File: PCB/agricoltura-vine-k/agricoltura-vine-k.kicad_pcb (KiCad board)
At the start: 4 copper layers, 110 x 80 mm, 110 parts, among them K1 G5LE-14_DC5, K2 G5LE-14_DC5, K3 G5LE-14_DC5, K4 G5LE-14_DC5, Q1 IRLML6346TRPBF, Q2 IRLML6346TRPBF, Q3 IRLML6346TRPBF, Q4 IRLML6346TRPBF, SW1 TL3301NF260QG, T1 BU2032SM-JJ-GTR, T16 0395121002, T17 0395121004, T18 0395121004, T19 TSW-108-07-G-T, T2 20021121-00010C4LF, T20 0010897080, T3 0675031020, T4 0395121006, T5 0395121006, U1 STM32F446RET6, U10 ZXGD3009E6TA, U2 ZXGD3009E6TA, U3 ZXGD3009E6TA, U4 AP63203WU-7, U5 AP63205WU-7, U6 MAX13450EAUD+, U7 MAX13450EAUD+, U8 TCA6416ARTWR, U9 ZXGD3009E6TA, X1 ABM3B-8.000MHZ-B2-T, X2 ABS07-32.768KHZ-9-T

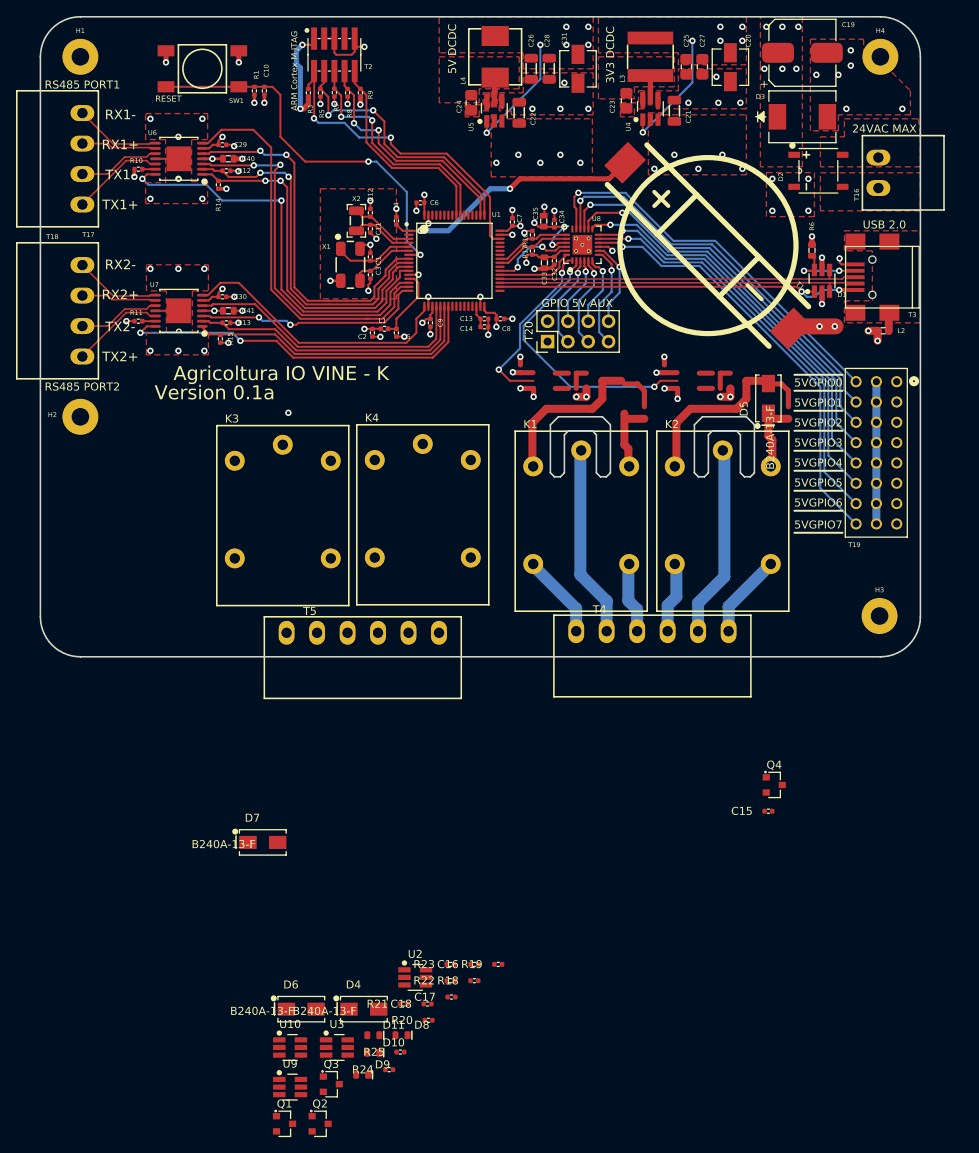
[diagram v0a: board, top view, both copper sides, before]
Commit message: PCB Routing PRogress
5th relay added to schematic, PCB section with Relays routed, still need to connecto IO expander channels.
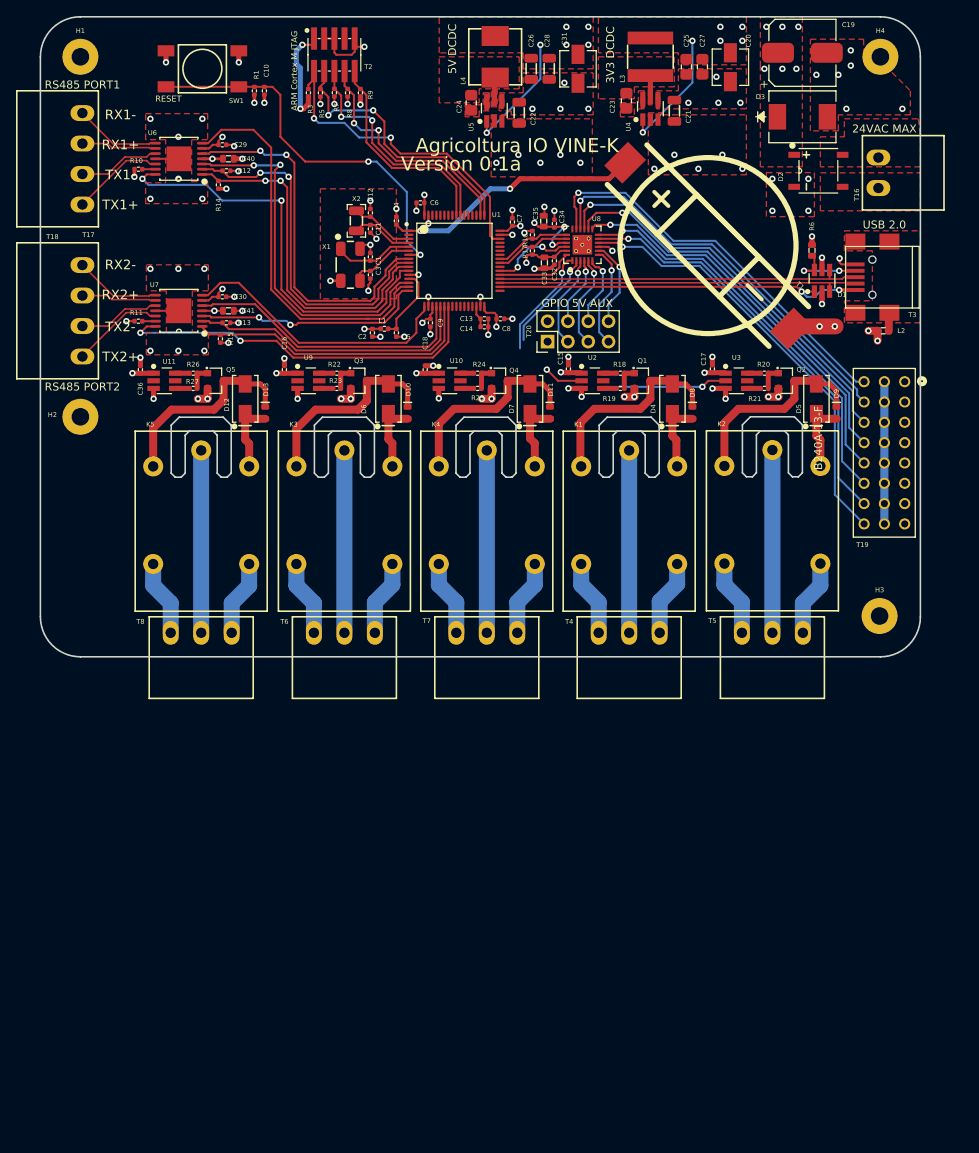
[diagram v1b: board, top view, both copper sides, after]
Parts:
- added C36: C0402C104K9PACTU, AVR-KiCAD-Lib-Resistors:R0402, F.Cu at (117.5, 104.1)
- added D12: B240A-13-F, AVR-KiCAD-Lib-Diodes:B240A-13-F, F.Cu at (130.6, 107.8)
- added D13: LTST-C194TBKT, AVR-KiCAD-Lib-Diodes:LED0603, F.Cu at (133.1, 109.5)
- added K5: G5LE-14_DC5, AVR-KiCAD-Lib-Relays-Contactors:G5LE-14_DC5, F.Cu at (125.1, 122.3)
- added Q5: IRLML6346TRPBF, AVR-KiCAD-Lib-Transistors:SOT-23, F.Cu at (126.9, 105.5)
- added R26: RC0402FR-0710RL, AVR-KiCAD-Lib-Resistors:R0402, F.Cu at (124.1, 104.5)
- added R27: RC0402FR-0710RL, AVR-KiCAD-Lib-Resistors:R0402, F.Cu at (124.1, 106.5)
- added T6: 0395121003, AVR-KiCAD-Lib-Connectors:0395121003, F.Cu at (143.0, 137.0)
- added T7: 0395121003, AVR-KiCAD-Lib-Connectors:0395121003, F.Cu at (160.8, 137.0)
- added T8: 0395121003, AVR-KiCAD-Lib-Connectors:0395121003, F.Cu at (125.1, 137.0)
- added U11: ZXGD3009E6TA, growbox-KiCAD-ICs:SOT-23-6_Handsoldering, F.Cu at (120.5, 105.5)
- T4, T5: value 0395121006 -> 0395121003; footprint AVR-KiCAD-Lib-Connectors:0395121006 -> AVR-KiCAD-Lib-Connectors:0395121003
- moved Q2 109.7 mm to (198.2, 105.5)
- moved Q1 103.1 mm to (180.2, 105.5)
- moved D9 101.8 mm to (204.5, 109.5), turned to 90 degrees
- moved U3 97.2 mm to (192.0, 105.5)
- moved R20 91.1 mm to (195.5, 104.5)
- moved R21 89.2 mm to (195.5, 106.5)
- moved U9 88.3 mm to (138.5, 105.5)
- moved Q3 88.0 mm to (144.8, 105.5)
- moved R24 87.8 mm to (159.7, 104.5)
- moved D8 85.9 mm to (186.5, 109.5), turned to 90 degrees
- moved U10 85.7 mm to (156.2, 105.5)
- moved D4 85.5 mm to (184.0, 107.8), turned to 90 degrees
- moved C17 85.0 mm to (189.0, 104.0), turned to 270 degrees
- moved R25 83.5 mm to (159.7, 106.5)
- moved D11 80.9 mm to (168.7, 109.5), turned to 90 degrees
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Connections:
- T5 pad 1: Net-(K3-Pad4) -> Net-(K2-Pad4)
- T5 pad 2: Net-(K3-Pad1) -> Net-(K2-Pad1)
- T5 pad 3: Net-(K3-Pad3) -> Net-(K2-Pad3)
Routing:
- net +5V: track 127.2 -> 189.3 mm, vias 13 -> 16
- net Net-(D12-Pad1): track 0.00 -> 25.3 mm
- net Net-(D10-Pad2): track 0.00 -> 25.2 mm
- net Net-(D11-Pad2): track 0.00 -> 25.2 mm
- net Net-(K5-Pad1): track 0.00 -> 22.8 mm
- net Net-(K4-Pad1): track 0.00 -> 22.8 mm
- net Net-(K3-Pad1): track 0.00 -> 22.8 mm
- net /5V IO Interfaces/DRV2: track 34.6 -> 12.7 mm, vias 2 -> 1
- net GND: track 83.0 -> 97.5 mm, vias 80 -> 92
- net /Relay Circuits/DRV2: track 0.00 -> 13.7 mm, vias 0 -> 1
- net Net-(K5-Pad4): track 0.00 -> 9.51 mm
- net Net-(K5-Pad3): track 0.00 -> 9.51 mm
- net Net-(K4-Pad4): track 0.00 -> 9.51 mm
- net Net-(K4-Pad3): track 0.00 -> 9.51 mm
- net Net-(K3-Pad4): track 0.00 -> 9.51 mm
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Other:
- outline, holes or cut-outs redrawn
- board text added: "Agricoltura IO VINE-K"
- board text removed: "5VGPIO0"
- board text removed: "5VGPIO1"
- board text removed: "5VGPIO2"
- board text removed: "5VGPIO3"
- board text removed: "5VGPIO4"
- board text removed: "5VGPIO5"
- board text removed: "5VGPIO6"
- board text removed: "5VGPIO7"
- board text removed: "Agricoltura IO VINE - K"

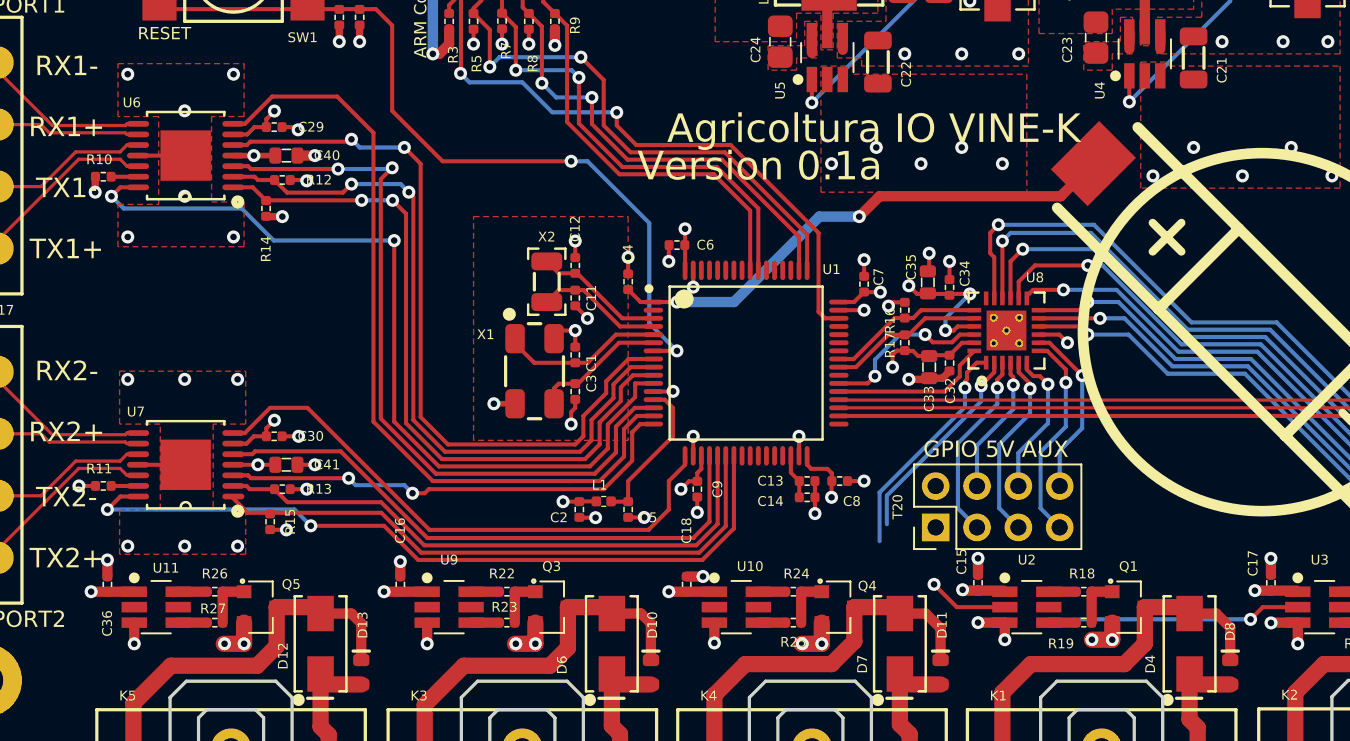
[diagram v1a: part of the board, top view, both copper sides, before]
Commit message: Finished
PCB routing complete, up for review before fab.
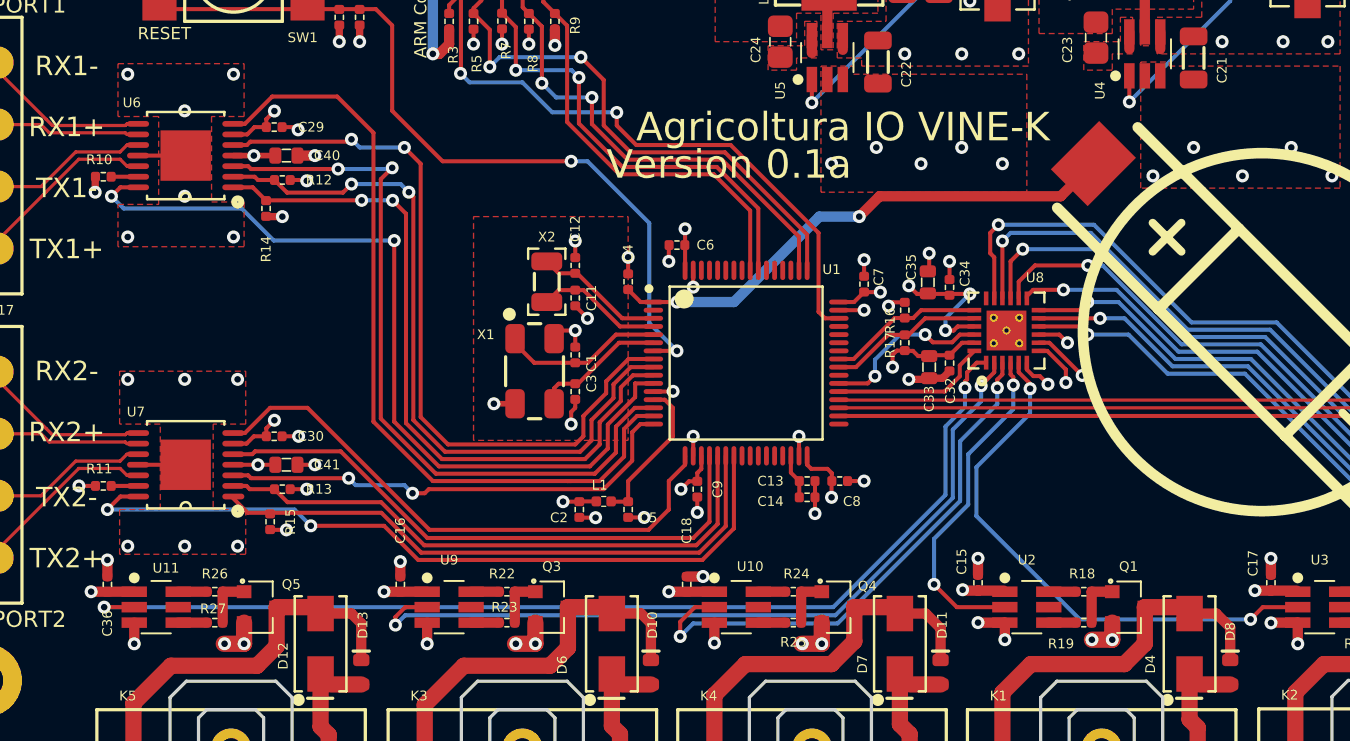
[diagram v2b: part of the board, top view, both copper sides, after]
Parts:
- removed T20: 0010897080, AVR-KiCAD-Lib-Connectors:Pin_Header_Straight_2x04_Pitch2.54mm
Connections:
- U10 pad 2: /Relay Circuits/DRV4 -> /5V IO Interfaces/DRV3
- U11 pad 2: Net-(U11-Pad2) -> /5V IO Interfaces/DRV5
- U2 pad 2: /Relay Circuits/DRV1 -> /5V IO Interfaces/DRV2
- U3 pad 2: /Relay Circuits/DRV2 -> /5V IO Interfaces/DRV1
- U8 pad 1: /5V IO Interfaces/DRV1 -> /5V IO Interfaces/DRV5
- U8 pad 2: /5V IO Interfaces/DRV2 -> /5V IO Interfaces/DRV4
- U8 pad 3: /5V IO Interfaces/P02 -> /5V IO Interfaces/DRV3
- U8 pad 4: /5V IO Interfaces/P03 -> /5V IO Interfaces/DRV2
- U8 pad 5: /5V IO Interfaces/P04 -> /5V IO Interfaces/DRV1
- U8 pad 6: /5V IO Interfaces/P05 -> Net-(U8-Pad6)
- U8 pad 7: /5V IO Interfaces/P06 -> Net-(U8-Pad7)
- U8 pad 8: /5V IO Interfaces/P07 -> Net-(U8-Pad8)
- U9 pad 2: /Relay Circuits/DRV3 -> /5V IO Interfaces/DRV4
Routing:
- net /5V IO Interfaces/DRV5: track 0.00 -> 65.9 mm, vias 0 -> 2
- net /5V IO Interfaces/DRV4: track 0.00 -> 49.6 mm, vias 0 -> 2
- net /5V IO Interfaces/DRV3: track 0.00 -> 33.6 mm, vias 0 -> 2
- net /5V IO Interfaces/DRV1: track 14.0 -> 33.8 mm, vias 1 -> 2
- net /Relay Circuits/DRV2: track 13.7 -> 0.00 mm, vias 1 -> 0
- net /5V IO Interfaces/P06: track 13.0 -> 0.00 mm, vias 1 -> 0
- net /5V IO Interfaces/P02: track 11.7 -> 0.00 mm, vias 1 -> 0
- net /5V IO Interfaces/P04: track 11.7 -> 0.00 mm, vias 1 -> 0
- net /5V IO Interfaces/P07: track 11.0 -> 0.00 mm, vias 1 -> 0
- net /5V IO Interfaces/P05: track 9.11 -> 0.00 mm, vias 1 -> 0
- net /5V IO Interfaces/P03: track 8.58 -> 0.00 mm, vias 1 -> 0
- net /5V IO Interfaces/DRV2: track 12.7 -> 20.6 mm, vias 1 -> 2
- net /Relay Circuits/DRV1: track 4.93 -> 0.00 mm, vias 1 -> 0
- net Net-(U8-Pad8): track 0.00 -> 3.51 mm, vias 0 -> 1
- net Net-(U8-Pad7): track 0.00 -> 2.95 mm, vias 0 -> 1
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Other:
- board text removed: "GPIO 5V AUX"

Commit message: EEPROM
added EEPROM to IO expander serial port. Broke out remaining IO expander pins to header. Adjusted silkscreen labeling and reset button position to match the other Vine.
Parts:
- added C37: C0805C103KCRACAUTO, AVR-KiCAD-Lib-Capacitors:C0805, F.Cu at (206.2, 100.5)
- added C38: C0402C104K9PACTU, AVR-KiCAD-Lib-Resistors:R0402, F.Cu at (171.0, 81.5)
- added D14: SMAJ30CA, AVR-KiCAD-Lib-Diodes:SMAJ30CA, F.Cu at (213.0, 101.5)
- added R2: RC0402FR-0722RL, AVR-KiCAD-Lib-Resistors:R0402, F.Cu at (166.5, 94.2)
- added R28: RC0402FR-0722RL, AVR-KiCAD-Lib-Resistors:R0402, F.Cu at (166.5, 93.0)
- added R29: RC1206FR-071ML, AVR-KiCAD-Lib-Resistors:R1206, F.Cu at (210.0, 101.2)
- added R30: RC0402FR-074K7L, AVR-KiCAD-Lib-Resistors:R0402, F.Cu at (165.0, 80.5)
- added R31: RC0402FR-074K7L, AVR-KiCAD-Lib-Resistors:R0402, F.Cu at (166.0, 82.5)
- added R4: RC0402FR-0710KL, AVR-KiCAD-Lib-Resistors:R0402, F.Cu at (166.5, 95.5)
- added T9: TSW-103-07-G-T, AVR-KiCAD-Lib-Connectors:TSW-103-07-G-T, F.Cu at (174.8, 99.2)
- added U12: AT24C16D-STUM-T, AVR-KiCAD-Lib-ICs:SOT-23-5, F.Cu at (168.5, 81.0)
- moved C10 6.41 mm to (127.0, 67.0)
- moved R1 6.41 mm to (125.8, 67.0)
- moved SW1 6.41 mm to (119.2, 64.2)
- moved T19 5.00 mm to (210.5, 119.5)
- moved L2 2.41 mm to (208.0, 99.8), turned to 270 degrees
- moved C15 0.56 mm to (170.8, 104.5)
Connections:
- U1 pad 34: /STM32F446RET Controller/VBUS -> /STM32F446RET Controller/MCU_VBUS
- U1 pad 35: /STM32F446RET Controller/D- -> /STM32F446RET Controller/MCU_D-
- U1 pad 36: /STM32F446RET Controller/D+ -> /STM32F446RET Controller/MCU_D+
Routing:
- net /5V IO Interfaces/IO_SCL: track 9.57 -> 26.3 mm, vias 0 -> 2
- net /5V IO Interfaces/IO_SDA: track 9.57 -> 25.7 mm, vias 0 -> 2
- net +3V3: track 65.4 -> 81.4 mm, vias 26 -> 29
- net /STM32F446RET Controller/NRST: track 48.6 -> 55.6 mm
- net Net-(T9-Pad9): track 2.10 -> 8.01 mm
- net Net-(T9-Pad6): track 2.95 -> 8.64 mm
- net Net-(T9-Pad3): track 3.51 -> 9.00 mm
- net /STM32F446RET Controller/VBUS: track 46.9 -> 42.6 mm
- net /STM32F446RET Controller/MCU_VBUS: track 0.00 -> 4.29 mm
- net /STM32F446RET Controller/MCU_D-: track 0.00 -> 4.00 mm
- net +5V: track 189.3 -> 193.3 mm
- net /STM32F446RET Controller/MCU_D+: track 0.00 -> 3.71 mm
- net /STM32F446RET Controller/D-: track 45.5 -> 42.0 mm
- net /STM32F446RET Controller/D+: track 45.6 -> 42.4 mm
- net /5V IO Interfaces/DRV5: track 65.9 -> 63.2 mm
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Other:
- board text added: "5V GPIO"
- board text added: "JTAG"

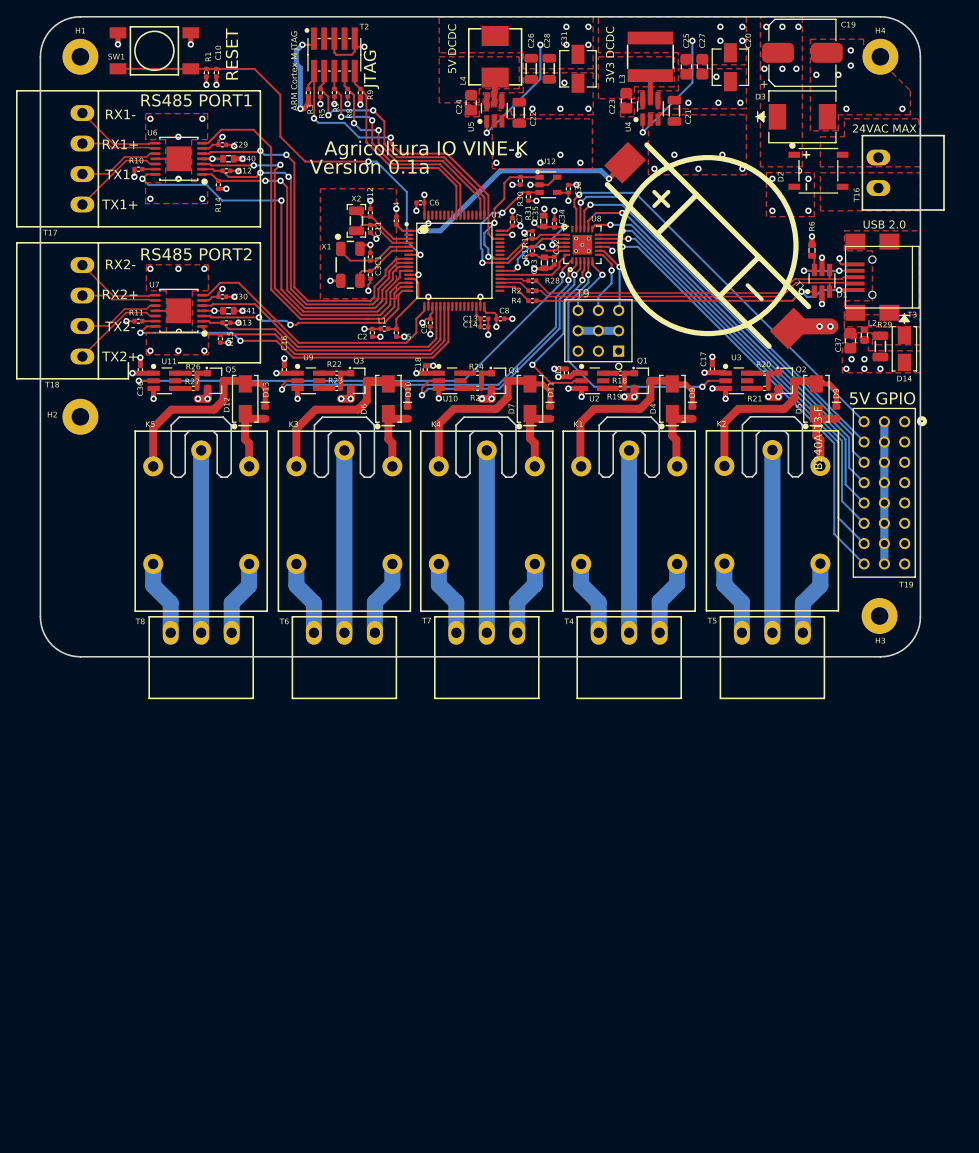
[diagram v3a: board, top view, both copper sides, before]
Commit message: PCB Tweaks
PCB tweaked for packaging in water resistant housing for greenhouse deployment
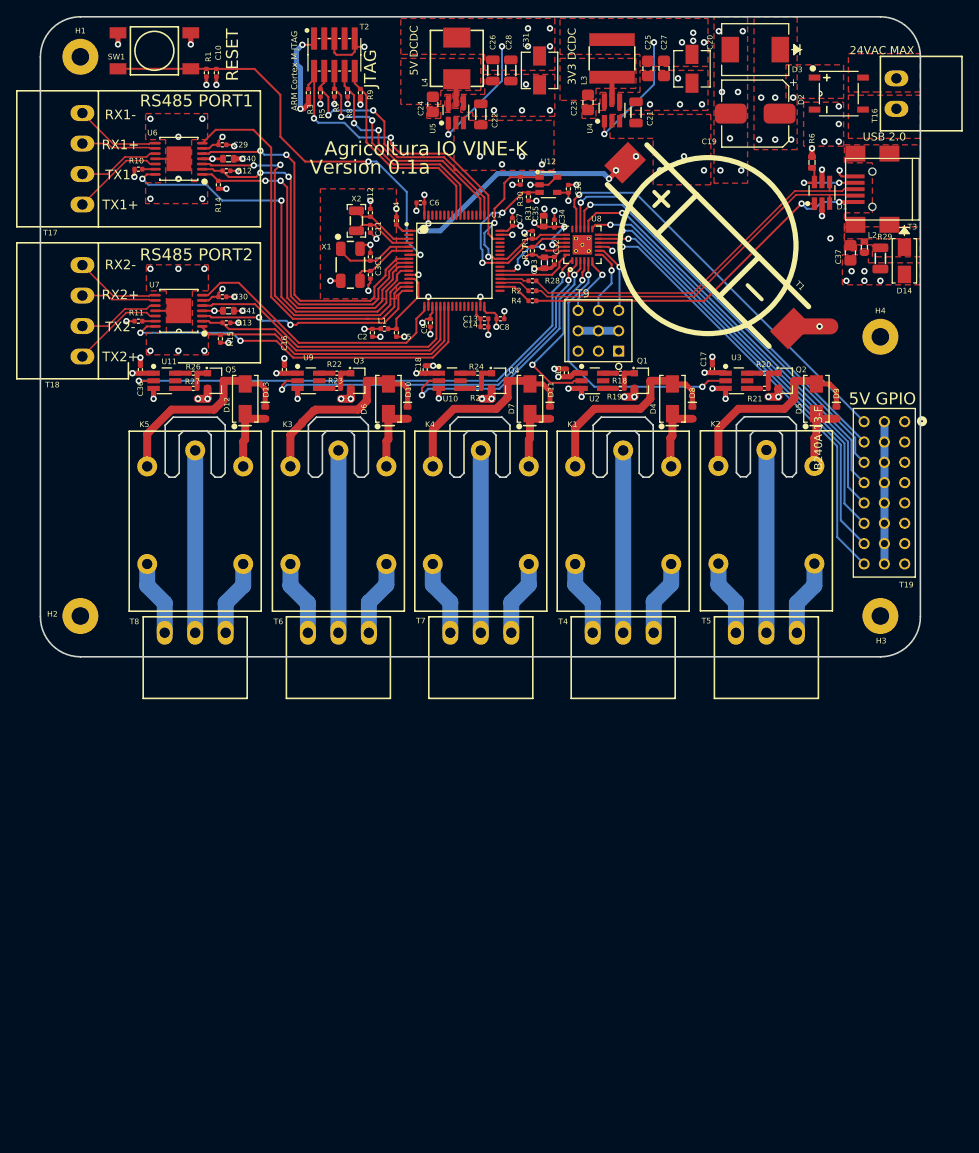
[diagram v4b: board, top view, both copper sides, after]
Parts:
- moved H4 35.0 mm to (210.0, 100.0)
- moved H2 24.9 mm to (110.0, 132.4)
- moved C37 11.0 mm to (206.2, 89.5)
- moved D1 11.0 mm to (202.7, 82.0)
- moved D14 11.0 mm to (213.0, 90.5)
- moved L2 11.0 mm to (208.0, 88.8)
- moved R29 11.0 mm to (210.0, 90.2)
- moved R6 11.0 mm to (201.4, 78.2)
- moved T3 11.0 mm to (209.0, 81.5)
- moved D3 10.3 mm to (194.3, 64.1), turned to 180 degrees
- moved T16 10.2 mm to (212.0, 69.6)
- moved D2 9.98 mm to (204.8, 69.6)
- moved C19 9.62 mm to (194.3, 72.1), turned to 180 degrees
- moved C20 4.80 mm to (186.4, 66.5)
- moved C21 4.80 mm to (179.4, 72.0)
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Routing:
- net Earth: track 225.3 -> 256.3 mm
- net /STM32F446RET Controller/D-: track 42.0 -> 46.6 mm
- net /STM32F446RET Controller/VBUS: track 42.6 -> 47.1 mm
- net /STM32F446RET Controller/D+: track 42.4 -> 47.0 mm
- net /5V IO Interfaces/DRV5: track 63.2 -> 65.7 mm
- net +5V: track 193.3 -> 192.7 mm
- net /RS485 Interface/RS485_UART_RX1: track 49.6 -> 50.2 mm
- net /RS485 Interface/RS485_UART_TX1: track 46.3 -> 46.9 mm
- net /RS485 Interface/RS485_DE1: track 43.7 -> 44.2 mm
- net /RS485 Interface/RS485_RE1: track 44.7 -> 45.2 mm
- net /RS485 Interface/RS485_TERM_EN1: track 46.2 -> 46.7 mm
- net /STM32F446RET Controller/VBAT: track 33.3 -> 33.0 mm, vias 2 -> 4
- net GND: vias 97 -> 98
- net +24V: vias 16 -> 13
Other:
- outline, holes or cut-outs redrawn

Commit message: kICAD 8
Projected updated to KiCAD 8
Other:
- net class Default removed
